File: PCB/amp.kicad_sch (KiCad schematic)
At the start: 0 parts

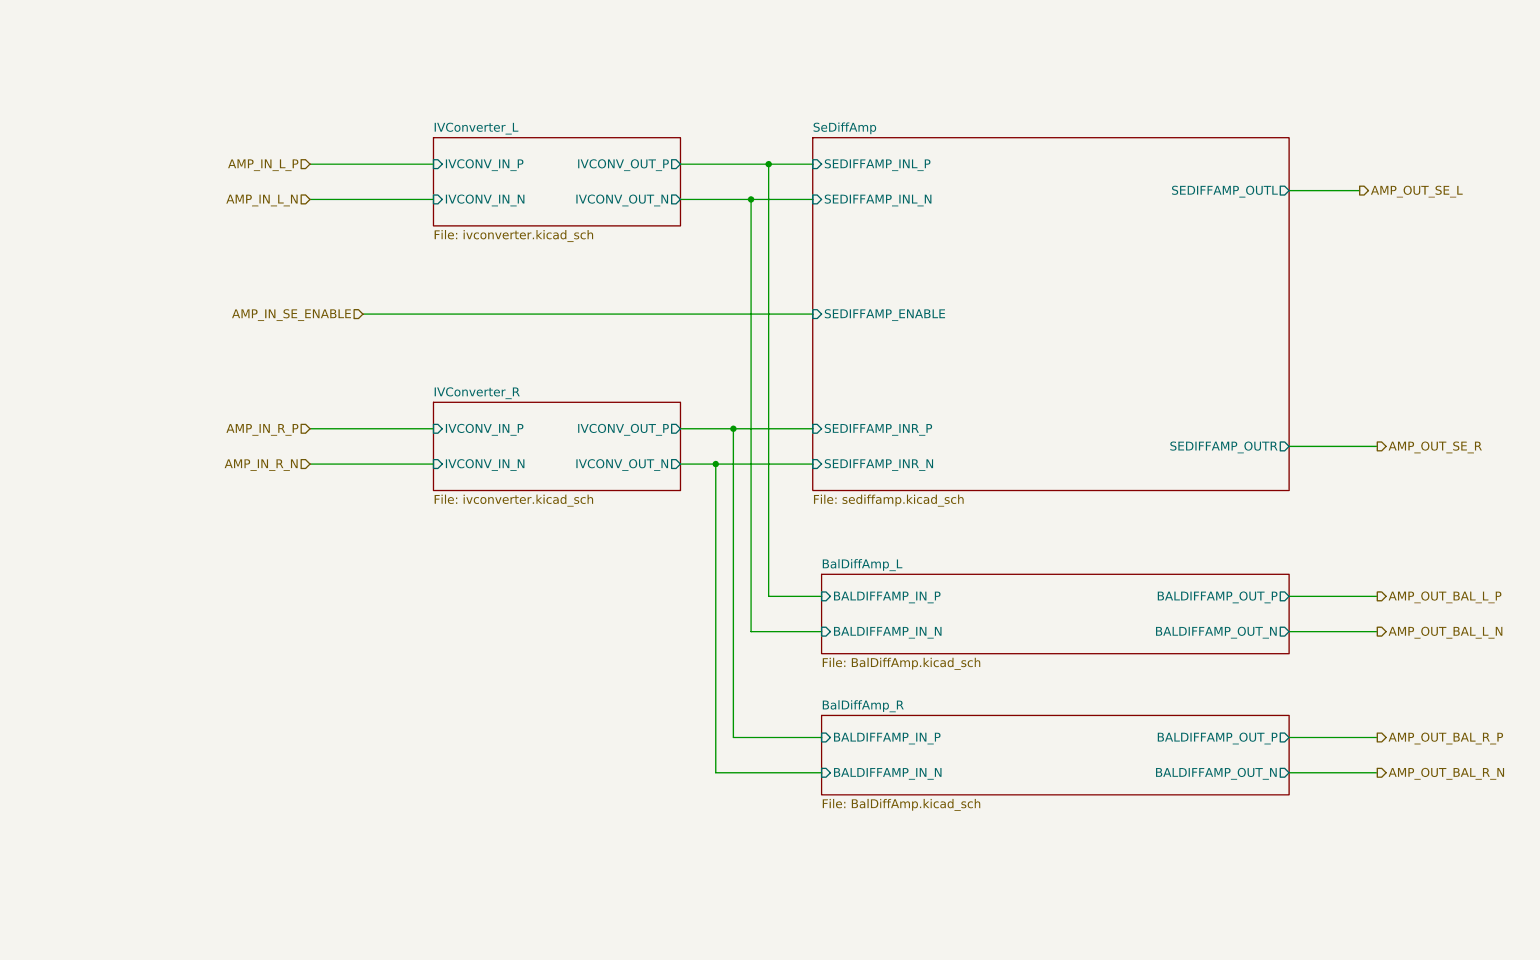
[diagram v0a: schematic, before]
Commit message: Added power supply and adjusted the AMP section to use only OPA1622 as output amp. In sync with Live 16
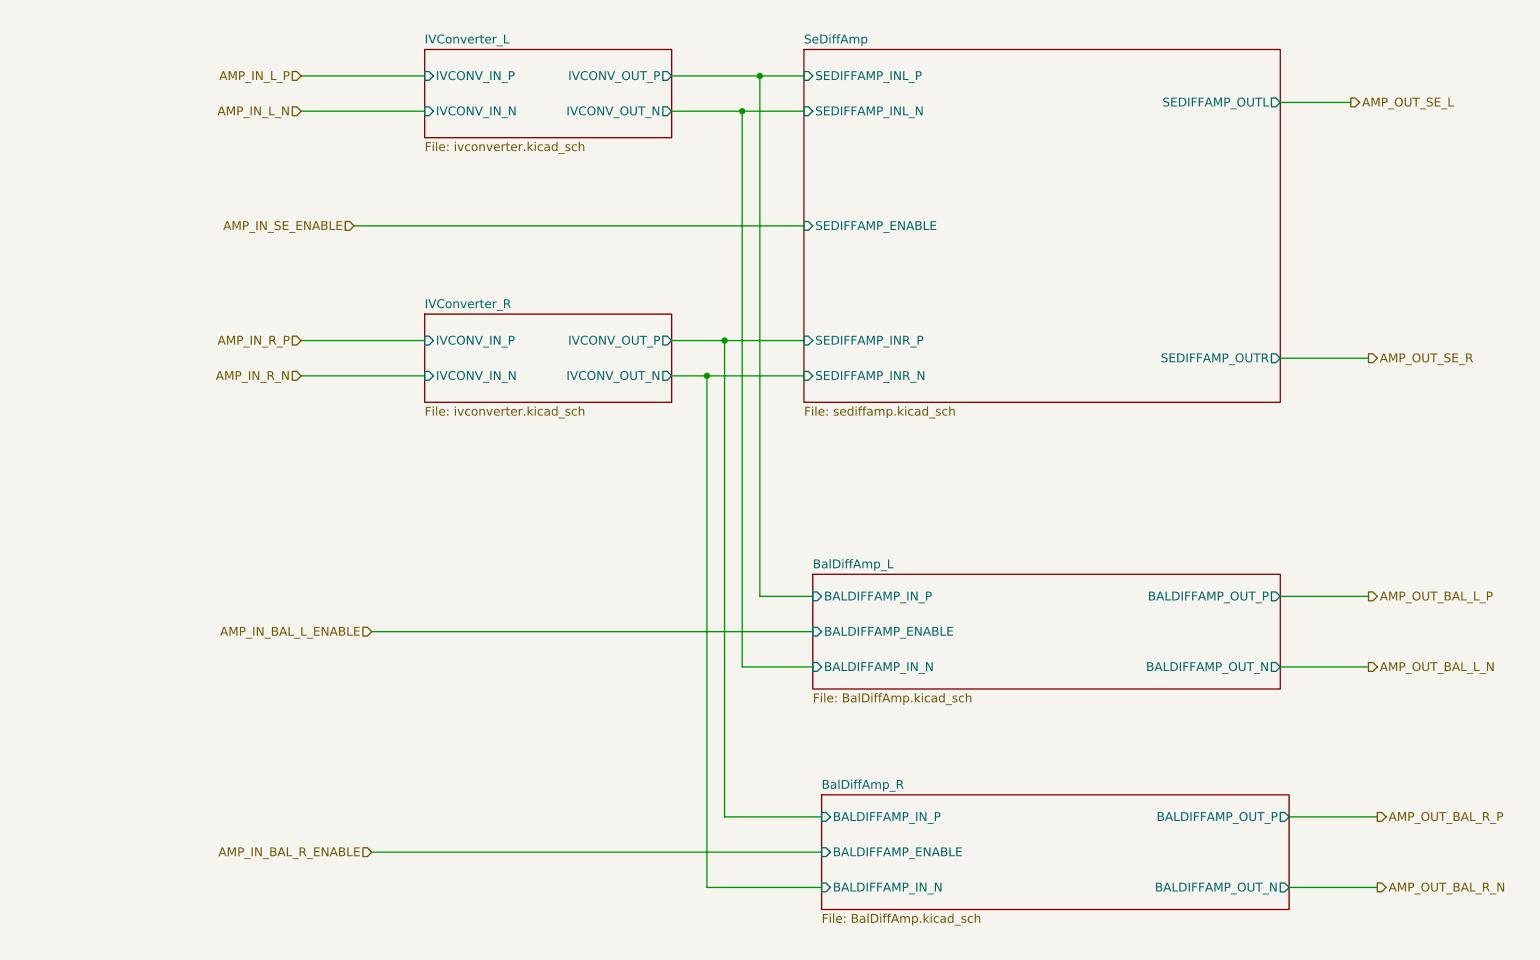
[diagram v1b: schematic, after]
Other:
- sheet BalDiffAmp_L ports: added BALDIFFAMP_ENABLE; removed none
- sheet BalDiffAmp_R ports: added BALDIFFAMP_ENABLE; removed none

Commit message: Added E2P and testpoints
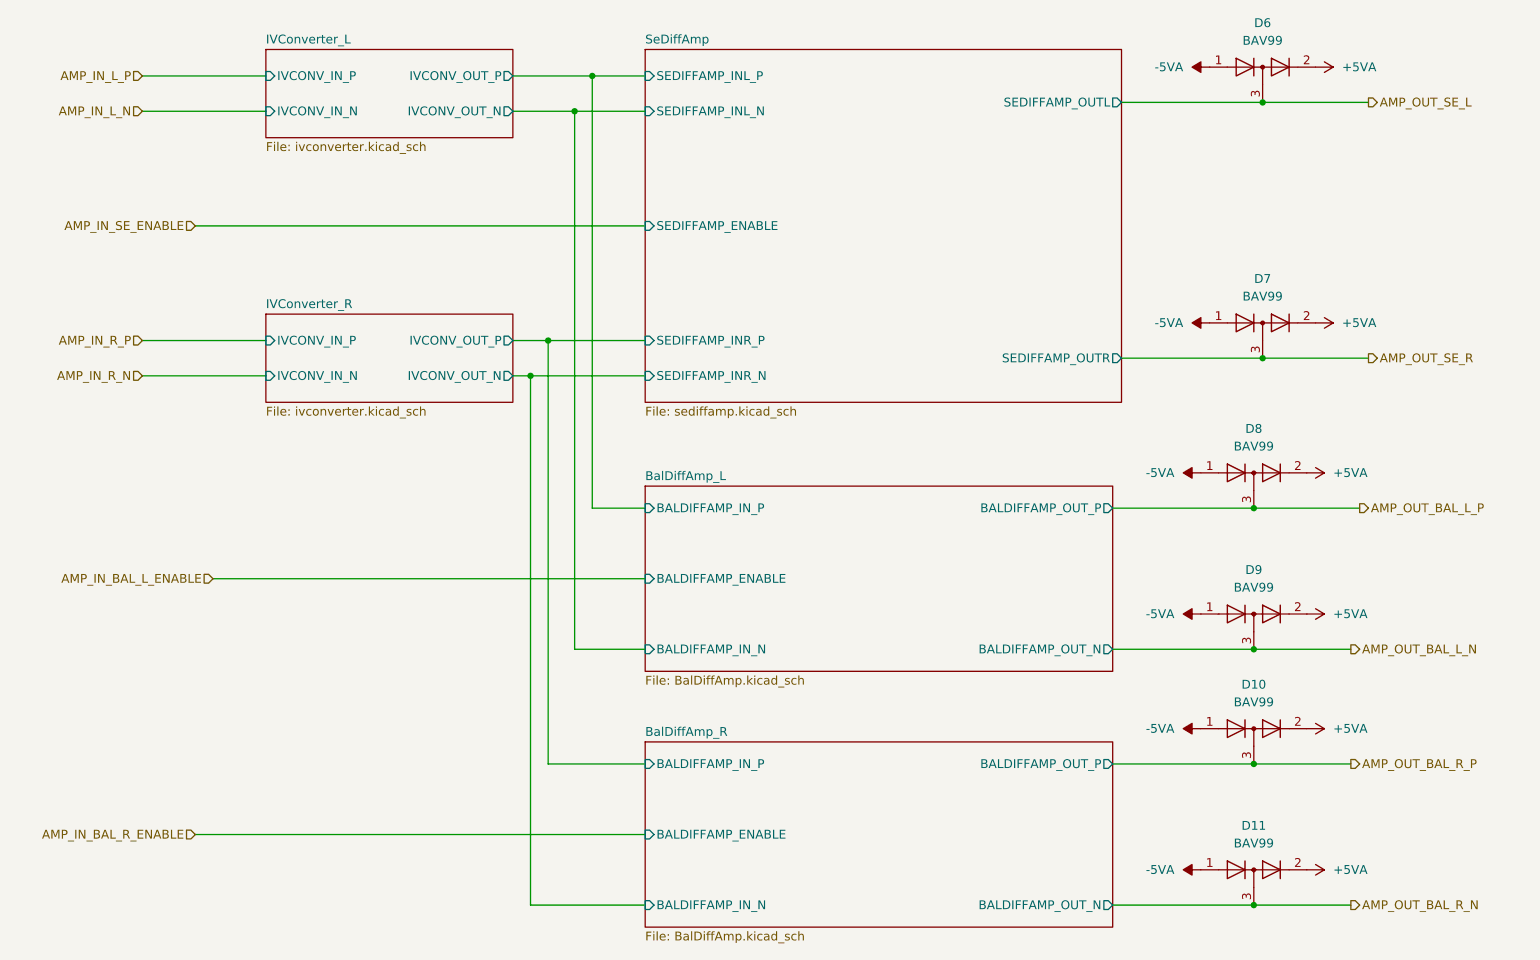
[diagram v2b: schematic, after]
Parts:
- added D10, D11, D6, D7, D8, D9: BAV99, Package_TO_SOT_SMD:SOT-23, symbol Diode:BAV99
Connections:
- net AMP_OUT_BAL_L_N: now also D9.3 (K)
- net AMP_OUT_BAL_L_P: now also D8.3 (K)
- net AMP_OUT_BAL_R_N: now also D11.3 (K)
- net AMP_OUT_BAL_R_P: now also D10.3 (K)
- net AMP_OUT_SE_L: now also D6.3 (K)
- net AMP_OUT_SE_R: now also D7.3 (K)
- new net +5VA: D10.2 (A), D11.2 (A), D6.2 (A), D7.2 (A), D8.2 (A), D9.2 (A)
- new net -5VA: D10.1 (K), D11.1 (K), D6.1 (K), D7.1 (K), D8.1 (K), D9.1 (K)

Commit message: Updated PCB with digital traxce suggestions. Added JLCPCB Pns
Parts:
- D10, D11, D6, D7, D8, D9: JLCPCBPn (none) -> C2500
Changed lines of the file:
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@@
+			)
+		)
+		(property "JLCPCBPn" "C2500"
+			(at 203.2 95.25 0)
+			(effects
+				(font
+					(size 1.27 1.27)
+				)
+				(hide yes)
 			)
 		)
@@
 			)
 		)
+		(property "JLCPCBPn" "C2500"
+			(at 203.2 132.08 0)
+			(effects
+				(font
+					(size 1.27 1.27)
+				)
+				(hide yes)
+			)
+		)
 		(pin "1"
 		)
@@
 			)
 		)
+		(property "JLCPCBPn" "C2500"
+			(at 203.2 152.4 0)
+			(effects
+				(font
+					(size 1.27 1.27)
+				)
+				(hide yes)
+			)
+		)
 		(pin "1"
 		)
@@
 			)
 		)
+		(property "JLCPCBPn" "C2500"
+			(at 203.2 115.57 0)
+			(effects
+				(font
+					(size 1.27 1.27)
+				)
+				(hide yes)
+			)
+		)
 		(pin "1"
 		)
@@
 			)
 		)
+		(property "JLCPCBPn" "C2500"
+			(at 204.47 73.66 0)
+			(effects
+				(font
+					(size 1.27 1.27)
+				)
+				(hide yes)
+			)
+		)
 		(pin "1"
 		)
@@
 			(at 204.47 36.83 0)
 			(effects
+				(font
+					(size 1.27 1.27)
+				)
+				(hide yes)
+			)
+		)
+		(property "JLCPCBPn" "C2500"
+			(at 204.47 36.83 0)
+			(effects

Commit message: Added filter capacitors to OPA1622 circuitry
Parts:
- D10, D11, D6, D7, D8, D9: JLCPCBPn C2500 -> (none); LCSC Part # (none) -> C2500
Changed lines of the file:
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@@
 			)
 		)
-		(property "JLCPCBPn" "C2500"
+		(property "LCSC Part #" "C2500"
 			(at 203.2 95.25 0)
 			(effects
@@
 			)
 		)
-		(property "JLCPCBPn" "C2500"
+		(property "LCSC Part #" "C2500"
 			(at 203.2 132.08 0)
 			(effects
@@
 			)
 		)
-		(property "JLCPCBPn" "C2500"
+		(property "LCSC Part #" "C2500"
 			(at 203.2 152.4 0)
 			(effects
@@
 			)
 		)
-		(property "JLCPCBPn" "C2500"
+		(property "LCSC Part #" "C2500"
 			(at 203.2 115.57 0)
 			(effects
@@
 			)
 		)
-		(property "JLCPCBPn" "C2500"
+		(property "LCSC Part #" "C2500"
 			(at 204.47 73.66 0)
 			(effects
@@
 			)
 		)
-		(property "JLCPCBPn" "C2500"
+		(property "LCSC Part #" "C2500"
 			(at 204.47 36.83 0)
 			(effects

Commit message: Redone placement and layout of OPA1622. Still finishing touches
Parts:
- added R65: 10k, Resistor_SMD:R_0402_1005Metric_Pad0.72x0.64mm_HandSolder, symbol Device:R
- added R66: 22R, Resistor_SMD:R_0402_1005Metric_Pad0.72x0.64mm_HandSolder, symbol Device:R
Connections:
- new net AMP_IN_BAL_ENABLE: R66.1
- new net BalDiffAmp_L/BALDIFFAMP_ENABLE: R65.2, R66.2
- new net GND: R65.1

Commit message: Changed the BOM field for JLCPCB to the original name instead of LCSC
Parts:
- D10, D11, D6, D7, D8, D9: JLCPCB Part # (none) -> C2500; LCSC Part # C2500 -> (none)
- R65: JLCPCB Part # (none) -> C25744; LCSC Part # C25744 -> (none)
- R66: JLCPCB Part # (none) -> C25092; LCSC Part # C25092 -> (none)
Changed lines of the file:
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@@
 			)
 		)
-		(property "LCSC Part #" "C2500"
+		(property "JLCPCB Part #" "C2500"
 			(at 203.2 95.25 0)
 			(effects
@@
 			)
 		)
-		(property "LCSC Part #" "C25744"
+		(property "JLCPCB Part #" "C25744"
 			(at 80.01 118.11 0)
 			(effects
@@
 			)
 		)
-		(property "LCSC Part #" "C2500"
+		(property "JLCPCB Part #" "C2500"
 			(at 203.2 132.08 0)
 			(effects
@@
 			)
 		)
-		(property "LCSC Part #" "C25092"
+		(property "JLCPCB Part #" "C25092"
 			(at 60.96 110.49 0)
 			(effects
@@
 			)
 		)
-		(property "LCSC Part #" "C2500"
+		(property "JLCPCB Part #" "C2500"
 			(at 203.2 152.4 0)
 			(effects
@@
 			)
 		)
-		(property "LCSC Part #" "C2500"
+		(property "JLCPCB Part #" "C2500"
 			(at 203.2 115.57 0)
 			(effects
@@
 			)
 		)
-		(property "LCSC Part #" "C2500"
+		(property "JLCPCB Part #" "C2500"
 			(at 204.47 73.66 0)
 			(effects
@@
 			)
 		)
-		(property "LCSC Part #" "C2500"
+		(property "JLCPCB Part #" "C2500"
 			(at 204.47 36.83 0)
 			(effects
